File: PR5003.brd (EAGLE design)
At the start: 52.8 x 37.8 mm, 38 parts, among them J1 AVR_SPI_PRG_6NS, U1 MIC5219 3.3V, U2 SI470X, U3 TPA2005D1DGN, Y1 32.768KHz

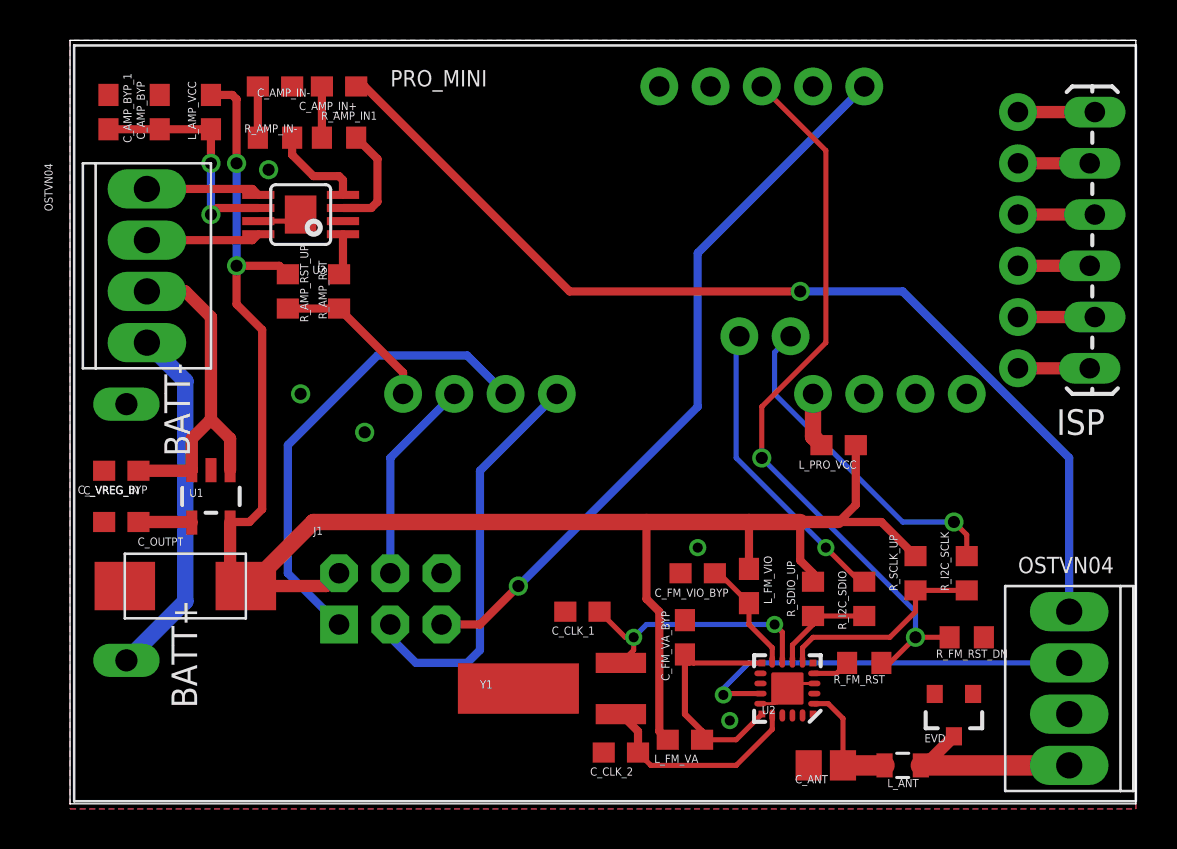
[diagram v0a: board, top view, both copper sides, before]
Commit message: part ordered from OSHPark ixjqvHyB
few revisions:

moved a bunch of shit away from the antenna
removed ground planes away from antenna

this commit has the version of PR5003 that we actually ordered from
OSHPark on 2014.01.27
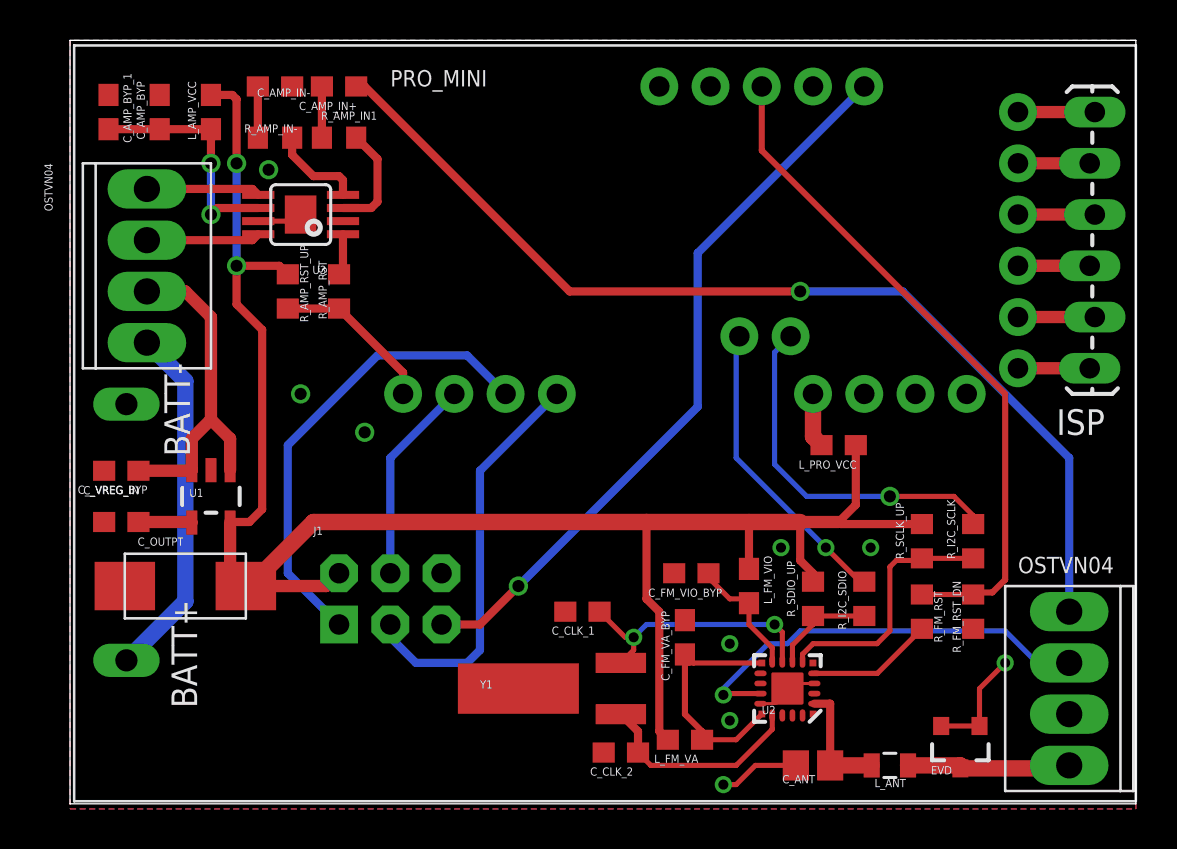
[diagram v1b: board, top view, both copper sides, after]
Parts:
- moved R_FM_RST 3.82 mm to (42.2, 9.53), turned to 270 degrees
- moved EVD 1.62 mm to (44.1, 2.86)
- moved R_SCLK_UP 1.62 mm to (42.2, 13.0)
- moved R_I2C_SCLK 1.62 mm to (44.8, 13.0)
- moved R_FM_RST_DN 1.31 mm to (44.8, 9.53), turned to 90 degrees
- moved C_ANT 0.64 mm to (36.8, 1.91)
- moved L_ANT 0.63 mm to (40.6, 1.91)
- moved C_FM_VIO_BYP 0.32 mm to (30.8, 11.4)
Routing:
- net GND: track 13.0 -> 22.5 mm, vias 5 -> 9
- net N$4: track 1.84 -> 6.25 mm
- net N$23: track 37.0 -> 33.9 mm, vias 2 -> 0
- net N$6: track 10.6 -> 12.7 mm
- net N$5: track 16.7 -> 18.0 mm
- net FM_AUD_OUT: track 19.9 -> 21.2 mm
- net ANT: track 9.59 -> 8.29 mm
- net N$30: track 5.68 -> 6.18 mm
